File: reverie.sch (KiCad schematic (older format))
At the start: 14 parts

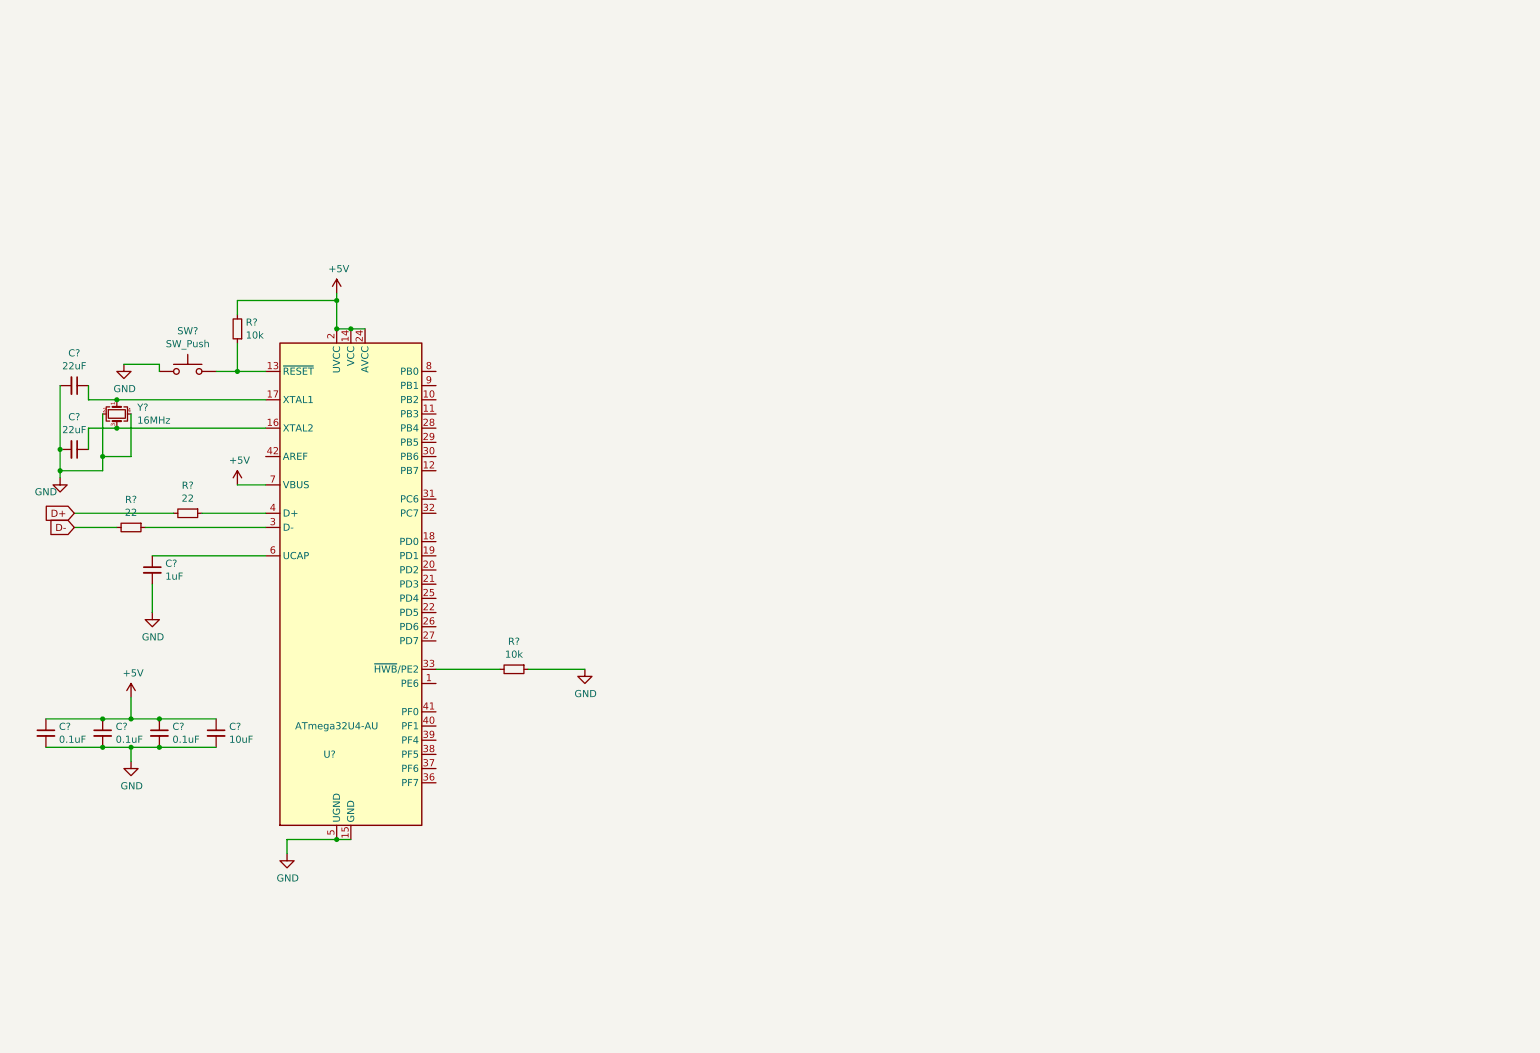
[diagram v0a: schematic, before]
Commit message: update schematic
add swtich matrix, usb, and esd circuits
assign footprints
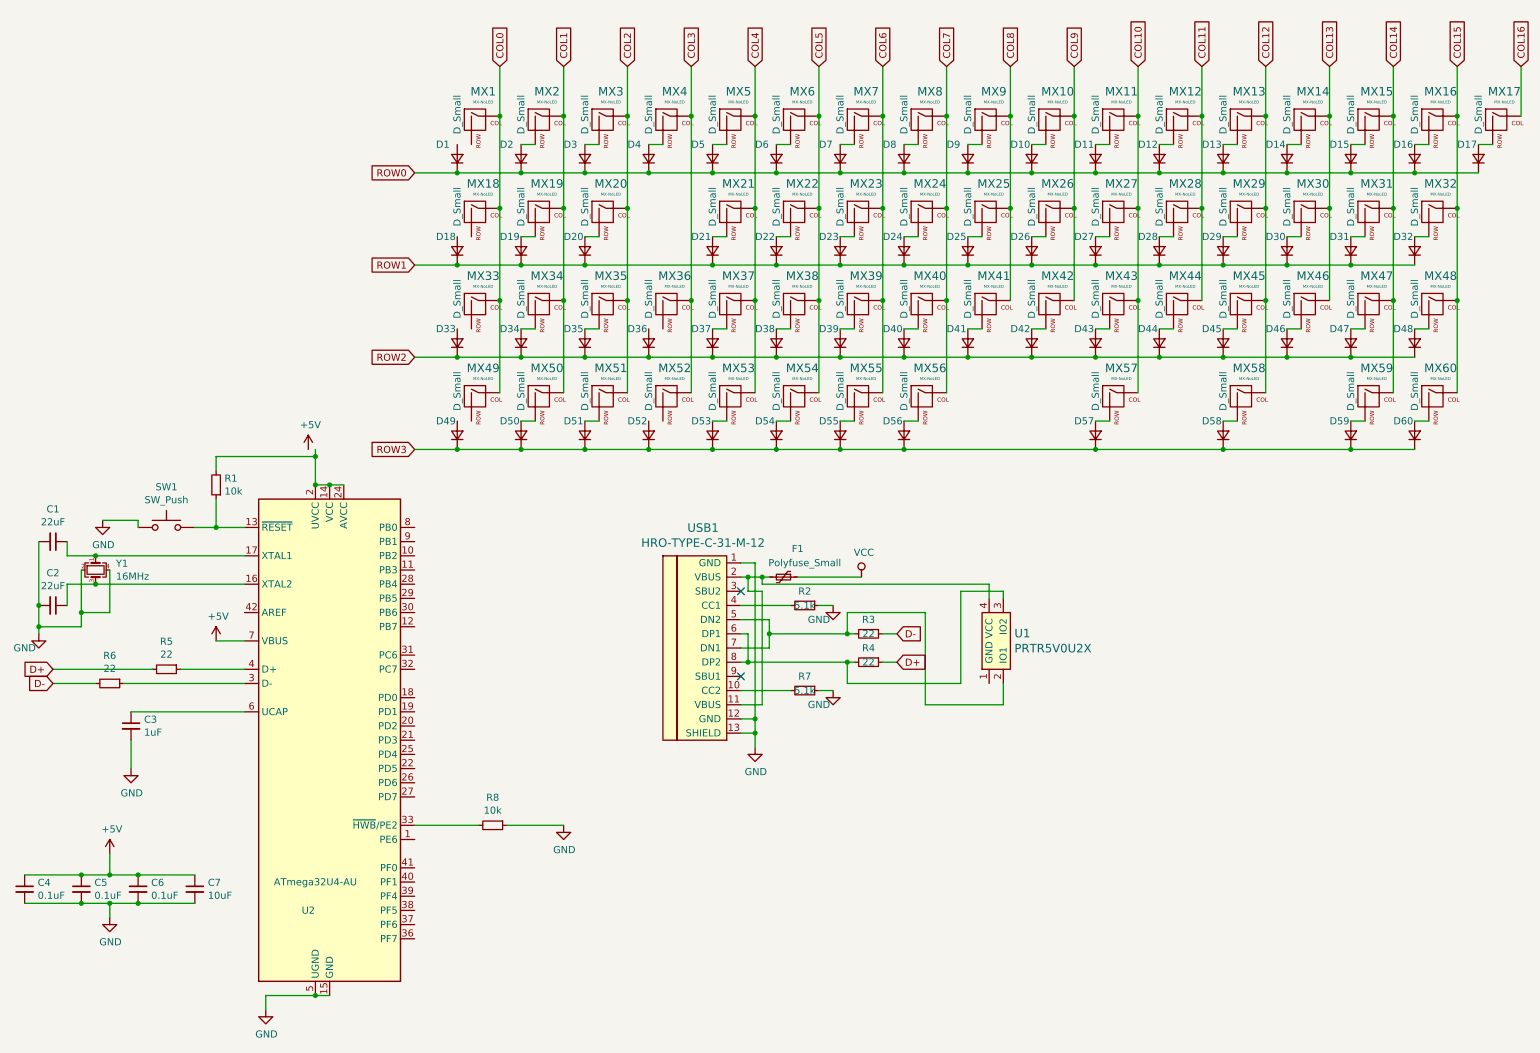
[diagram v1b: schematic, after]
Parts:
- added D1, D10, D11, D12, D13, D14, D15, D16, D17, D18, D19, D2, D20, D21, D22, D23, D24, D25, D26, D27, D28, D29, D3, D30, D31, D32, D33, D34, D35, D36, D37, D38, D39, D4, D40, D41, D42, D43, D44, D45, D46, D47, D48, D49, D5, D50, D51, D52, D53, D54, D55, D56, D57, D58, D59, D6, D60, D7, D8, D9: D_Small, Diode_SMD:D_SOD-123, symbol Device:D_Small
- added F1: Polyfuse_Small, MX_Only:MXOnly-1U-Hotswap, symbol Device:Polyfuse_Small
- added MX1, MX10, MX11, MX12, MX13, MX14, MX15, MX16, MX17, MX18, MX19, MX2, MX20, MX21, MX22, MX23, MX24, MX25, MX26, MX27, MX28, MX29, MX3, MX30, MX31, MX32, MX33, MX34, MX35, MX36, MX37, MX38, MX39, MX4, MX40, MX41, MX42, MX43, MX44, MX45, MX46, MX47, MX48, MX49, MX5, MX50, MX51, MX52, MX53, MX6, MX7, MX8, MX9: MX-NoLED, MX_Only:MXOnly-1U-Hotswap, symbol MX_Alps_Hybrid:MX-NoLED
- added MX54, MX55, MX58: MX-NoLED, MX_Only:MXOnly-1.5U-Hotswap, symbol MX_Alps_Hybrid:MX-NoLED
- added MX56: MX-NoLED, MX_Only:MXOnly-2.25U-Hotswap, symbol MX_Alps_Hybrid:MX-NoLED
- added MX57: MX-NoLED, MX_Only:MXOnly-2.75U-Hotswap, symbol MX_Alps_Hybrid:MX-NoLED
- added MX59, MX60: MX-NoLED, MX_Only:MXOnly-1.25U-Hotswap, symbol MX_Alps_Hybrid:MX-NoLED
- added R2, R7: 5.1k, Resistor_SMD:R_0805_2012Metric, symbol Device:R_Small
- added R3, R4: 22, Resistor_SMD:R_0805_2012Metric, symbol Device:R_Small
- added U1: PRTR5V0U2X, random-keyboard-parts:SOT143B, symbol random-keyboard-parts:PRTR5V0U2X
- added USB1: HRO-TYPE-C-31-M-12, Type-C:HRO-TYPE-C-31-M-12-HandSoldering, symbol Type-C:HRO-TYPE-C-31-M-12
- C1, C2, C3, C4, C5, C6, C7: renamed from C?; footprint (none) -> Capacitor_SMD:C_0805_2012Metric
- R1, R5, R6, R8: renamed from R?; footprint (none) -> Resistor_SMD:R_0805_2012Metric
- SW1: renamed from SW?; footprint (none) -> random-keyboard-parts:SKQG-1155865
- Y1: renamed from Y?; footprint (none) -> Crystal:Crystal_SMD_3225-4Pin_3.2x2.5mm
- gave numbers to parts that had none: 1
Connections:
- net +5V: no longer R1.2, U2.14 (VCC), U2.2 (UVCC), U2.24 (AVCC), U2.34 (VCC), U2.44 (AVCC)
- net D+: now also R4.1
- net D-: now also R3.1
- net GND: now also R2.1, R7.1, USB1.1 (GND), USB1.12 (GND), USB1.13 (SHIELD)
- new net: R1.2, U2.14 (VCC), U2.2 (UVCC), U2.24 (AVCC), U2.34 (VCC), U2.44 (AVCC)
- new net: D16.2 (A), MX16.2 (ROW)
- new net: D17.2 (A), MX17.2 (ROW)
- new net: D15.2 (A), MX15.2 (ROW)
- new net: D14.2 (A), MX14.2 (ROW)
- new net: D13.2 (A), MX13.2 (ROW)
- new net: D12.2 (A), MX12.2 (ROW)
- new net: D11.2 (A), MX11.2 (ROW)
- new net: D10.2 (A), MX10.2 (ROW)
- new net: D9.2 (A), MX9.2 (ROW)
- new net: D8.2 (A), MX8.2 (ROW)
- new net: D7.2 (A), MX7.2 (ROW)
- new net: D6.2 (A), MX6.2 (ROW)
- new net: D5.2 (A), MX5.2 (ROW)
- new net: D4.2 (A), MX4.2 (ROW)
- new net: D3.2 (A), MX3.2 (ROW)
- new net: D2.2 (A), MX2.2 (ROW)
- new net: D32.2 (A), MX32.2 (ROW)
- new net: D31.2 (A), MX31.2 (ROW)
- new net: D30.2 (A), MX30.2 (ROW)
- new net: D29.2 (A), MX29.2 (ROW)
- new net: D28.2 (A), MX28.2 (ROW)
- new net: D27.2 (A), MX27.2 (ROW)
- new net: D26.2 (A), MX26.2 (ROW)
- new net: D25.2 (A), MX25.2 (ROW)
- new net: D24.2 (A), MX24.2 (ROW)
- new net: D23.2 (A), MX23.2 (ROW)
- new net: D22.2 (A), MX22.2 (ROW)
- new net: D21.2 (A), MX21.2 (ROW)
- new net: D20.2 (A), MX20.2 (ROW)
- new net: D19.2 (A), MX19.2 (ROW)
- new net: D48.2 (A), MX48.2 (ROW)
- new net: D47.2 (A), MX47.2 (ROW)
- new net: D46.2 (A), MX46.2 (ROW)
- new net: D45.2 (A), MX45.2 (ROW)
- new net: D44.2 (A), MX44.2 (ROW)
- new net: D43.2 (A), MX43.2 (ROW)
- new net: D42.2 (A), MX42.2 (ROW)
- new net: D41.2 (A), MX41.2 (ROW)
- new net: D40.2 (A), MX40.2 (ROW)
- new net: D39.2 (A), MX39.2 (ROW)
- new net: D38.2 (A), MX38.2 (ROW)
- new net: D37.2 (A), MX37.2 (ROW)
- new net: D35.2 (A), MX35.2 (ROW)
- new net: D34.2 (A), MX34.2 (ROW)
- new net: D60.2 (A), MX60.2 (ROW)
- new net: D59.2 (A), MX59.2 (ROW)
- new net: D58.2 (A), MX58.2 (ROW)
- new net: D57.2 (A), MX57.2 (ROW)
- new net: D56.2 (A), MX56.2 (ROW)
- new net: D55.2 (A), MX55.2 (ROW)
- new net: D54.2 (A), MX54.2 (ROW)
- new net: D53.2 (A), MX53.2 (ROW)
- new net: D51.2 (A), MX51.2 (ROW)
- new net: D50.2 (A), MX50.2 (ROW)
- new net: R7.2, USB1.10 (CC2)
- new net: F1.2, U1.4 (VCC), USB1.11 (VBUS), USB1.2 (VBUS)
- new net: R2.2, USB1.4 (CC1)
- new net: R3.2, U1.2 (IO1), USB1.5 (DN2), USB1.7 (DN1)
- new net: R4.2, U1.3 (IO2), USB1.6 (DP1), USB1.8 (DP2)
- new net COL0: MX1.1 (COL), MX18.1 (COL), MX33.1 (COL), MX49.1 (COL)
- new net COL1: MX19.1 (COL), MX2.1 (COL), MX34.1 (COL), MX50.1 (COL)
- new net COL10: MX11.1 (COL), MX27.1 (COL), MX43.1 (COL), MX57.1 (COL)
- new net COL11: MX12.1 (COL), MX28.1 (COL), MX44.1 (COL)
- new net COL12: MX13.1 (COL), MX29.1 (COL), MX45.1 (COL), MX58.1 (COL)
- new net COL13: MX14.1 (COL), MX30.1 (COL), MX46.1 (COL)
- new net COL14: MX15.1 (COL), MX31.1 (COL), MX47.1 (COL), MX59.1 (COL)
- new net COL15: MX16.1 (COL), MX32.1 (COL), MX48.1 (COL), MX60.1 (COL)
- new net COL16: MX17.1 (COL)
- new net COL2: MX20.1 (COL), MX3.1 (COL), MX35.1 (COL), MX51.1 (COL)
- new net COL3: MX36.1 (COL), MX4.1 (COL), MX52.1 (COL)
- new net COL4: MX21.1 (COL), MX37.1 (COL), MX5.1 (COL), MX53.1 (COL)
- new net COL5: MX22.1 (COL), MX38.1 (COL), MX54.1 (COL), MX6.1 (COL)
- new net COL6: MX23.1 (COL), MX39.1 (COL), MX55.1 (COL), MX7.1 (COL)
- new net COL7: MX24.1 (COL), MX40.1 (COL), MX56.1 (COL), MX8.1 (COL)
- new net COL8: MX25.1 (COL), MX41.1 (COL), MX9.1 (COL)
- new net COL9: MX10.1 (COL), MX26.1 (COL), MX42.1 (COL)
- new net ROW0: D1.1 (K), D10.1 (K), D11.1 (K), D12.1 (K), D13.1 (K), D14.1 (K), D15.1 (K), D16.1 (K), D17.1 (K), D2.1 (K), D3.1 (K), D4.1 (K), D5.1 (K), D6.1 (K), D7.1 (K), D8.1 (K), D9.1 (K)
- new net ROW1: D18.1 (K), D19.1 (K), D20.1 (K), D21.1 (K), D22.1 (K), D23.1 (K), D24.1 (K), D25.1 (K), D26.1 (K), D27.1 (K), D28.1 (K), D29.1 (K), D30.1 (K), D31.1 (K), D32.1 (K)
- new net ROW2: D33.1 (K), D34.1 (K), D35.1 (K), D36.1 (K), D37.1 (K), D38.1 (K), D39.1 (K), D40.1 (K), D41.1 (K), D42.1 (K), D43.1 (K), D44.1 (K), D45.1 (K), D46.1 (K), D47.1 (K), D48.1 (K)
- new net ROW3: D49.1 (K), D50.1 (K), D51.1 (K), D52.1 (K), D53.1 (K), D54.1 (K), D55.1 (K), D56.1 (K), D57.1 (K), D58.1 (K), D59.1 (K), D60.1 (K)
- new net VCC: F1.1
- no-connect marks 0 -> 2
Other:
- moved on the sheet: C1, C2, C3, C4, C5, C6, C7, R1, R5, R6, R8, SW1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

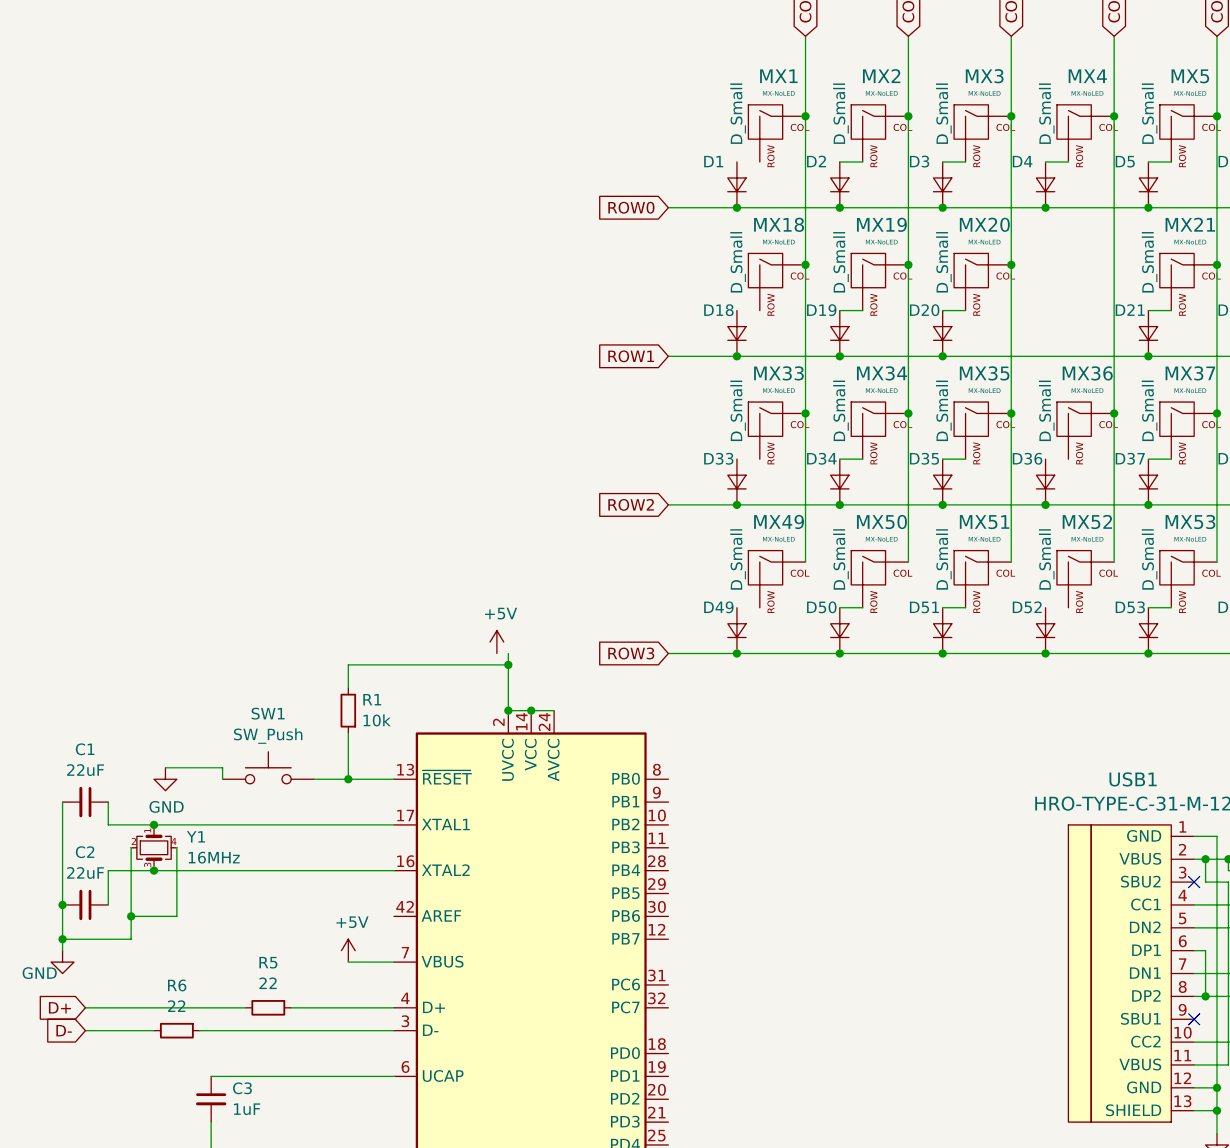
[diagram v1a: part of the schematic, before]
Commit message: align diodes on pcb
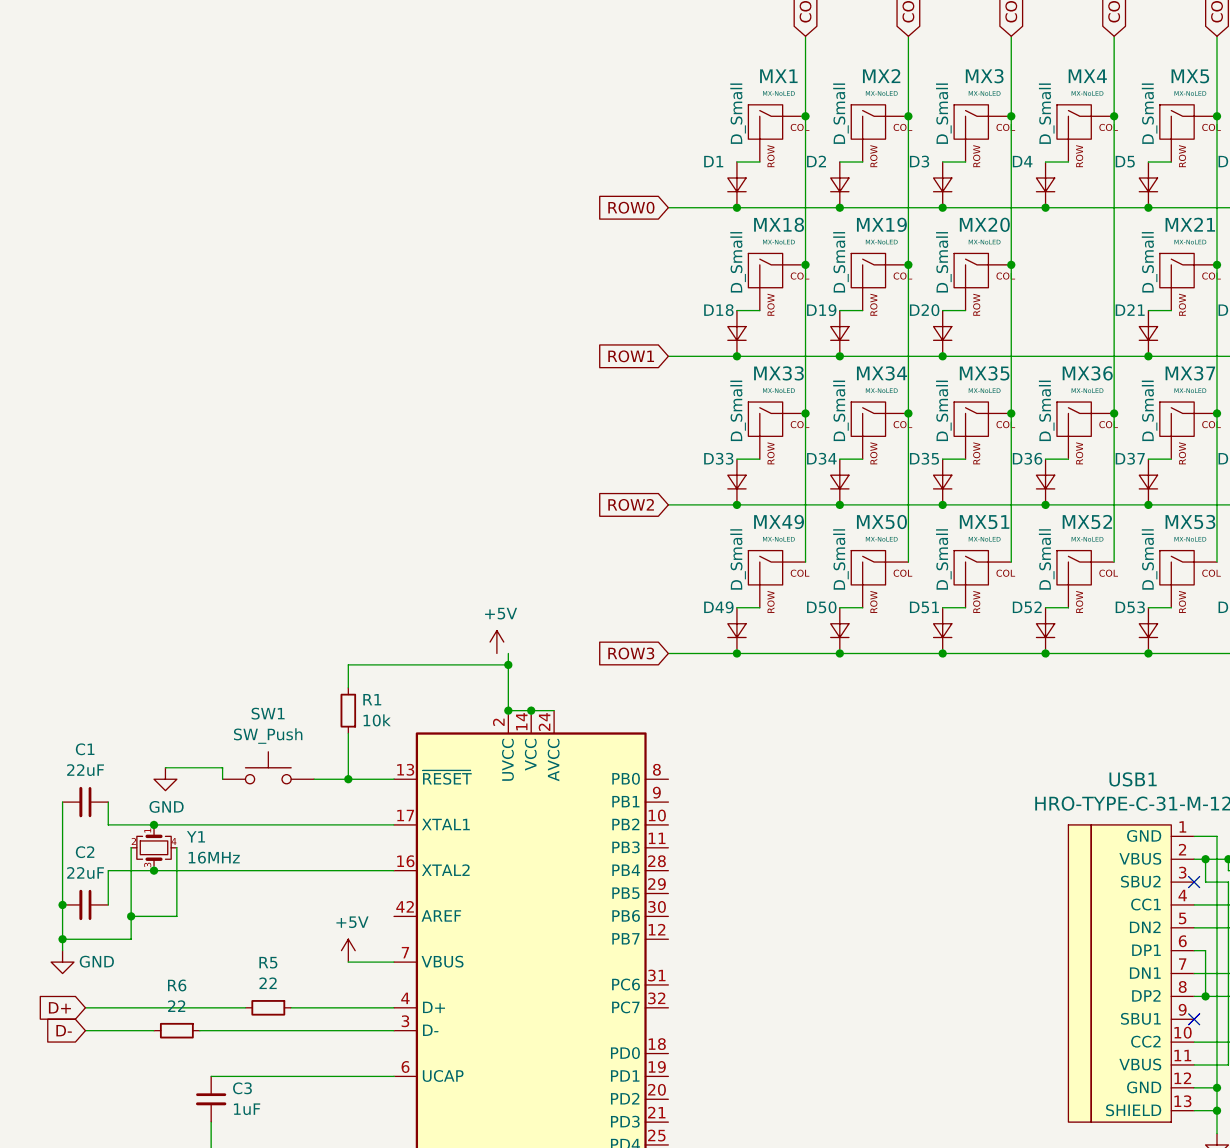
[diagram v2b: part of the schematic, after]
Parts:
- F1: footprint MX_Only:MXOnly-1U-Hotswap -> Fuse:Fuse_1206_3216Metric
- MX21, MX48: footprint MX_Only:MXOnly-1U-Hotswap -> MX_Only:MXOnly-1.25U-Hotswap
- MX32, MX37: footprint MX_Only:MXOnly-1U-Hotswap -> MX_Only:MXOnly-1.75U-Hotswap
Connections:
- net at MX1.2 (ROW): now also D1.2 (A)
- net at MX18.2 (ROW): now also D18.2 (A)
- net at MX33.2 (ROW): now also D33.2 (A)
- net at MX36.2 (ROW): now also D36.2 (A)
- net at MX49.2 (ROW): now also D49.2 (A)
- net at MX52.2 (ROW): now also D52.2 (A)
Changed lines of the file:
@@
 P 700 4800
 F 0 "#PWR0108" H 700 4550 50  0001 C CNN
-F 1 "GND" H 600 4700 50  0000 C CNN
+F 1 "GND" H 850 4750 50  0000 C CNN
 F 2 "" H 700 4800 50  0001 C CNN
 F 3 "" H 700 4800 50  0001 C CNN
@@
 F 0 "MX32" H 10583 2073 60  0000 C CNN
 F 1 "MX-NoLED" H 10583 1999 20  0000 C CNN
-F 2 "MX_Only:MXOnly-1U-Hotswap" H 9925 1825 60  0001 C CNN
+F 2 "MX_Only:MXOnly-1.75U-Hotswap" H 9925 1825 60  0001 C CNN
 F 3 "" H 9925 1825 60  0001 C CNN
 	1    10550 1850
@@
 F 0 "MX21" H 5633 2073 60  0000 C CNN
 F 1 "MX-NoLED" H 5633 1999 20  0000 C CNN
-F 2 "MX_Only:MXOnly-1U-Hotswap" H 4975 1825 60  0001 C CNN
+F 2 "MX_Only:MXOnly-1.25U-Hotswap" H 4975 1825 60  0001 C CNN
 F 3 "" H 4975 1825 60  0001 C CNN
 	1    5600 1850
@@
 F 0 "MX48" H 10583 2723 60  0000 C CNN
 F 1 "MX-NoLED" H 10583 2649 20  0000 C CNN
-F 2 "MX_Only:MXOnly-1U-Hotswap" H 9925 2475 60  0001 C CNN
+F 2 "MX_Only:MXOnly-1.25U-Hotswap" H 9925 2475 60  0001 C CNN
 F 3 "" H 9925 2475 60  0001 C CNN
 	1    10550 2500
@@
 F 0 "MX37" H 5633 2723 60  0000 C CNN
 F 1 "MX-NoLED" H 5633 2649 20  0000 C CNN
-F 2 "MX_Only:MXOnly-1U-Hotswap" H 4975 2475 60  0001 C CNN
+F 2 "MX_Only:MXOnly-1.75U-Hotswap" H 4975 2475 60  0001 C CNN
 F 3 "" H 4975 2475 60  0001 C CNN
 	1    5600 2500
@@
 F 0 "F1" V 5750 4500 50  0000 C CNN
 F 1 "Polyfuse_Small" V 5850 4550 50  0000 C CNN
-F 2 "MX_Only:MXOnly-1U-Hotswap" H 6000 4200 50  0001 L CNN
+F 2 "Fuse:Fuse_1206_3216Metric" H 6000 4200 50  0001 L CNN
 F 3 "~" H 5950 4400 50  0001 C CNN
 	1    5950 4400
@@
 Wire Wire Line
 	5700 4400 5650 4400
+Wire Wire Line
+	3650 1350 3750 1350
+Wire Wire Line
+	3650 2000 3750 2000
+Wire Wire Line
+	3650 2650 3750 2650
+Wire Wire Line
+	3650 3300 3750 3300
+Wire Wire Line
+	5100 3300 5000 3300
+Wire Wire Line
+	5100 2650 5000 2650
 $EndSCHEMATC
